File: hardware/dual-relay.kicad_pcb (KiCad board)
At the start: 2 copper layers, 45 x 45 mm, 34 parts, among them J1 AKL_5_2, J2 AKL_5_2, J3 AKL_5_2, P1 CON-SENSOR, Q1 2N7002P, Q2 2N7002P, U1 M24C64, U2 ORWH-SX, U3 ORWH-SX, U4 CM1293A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

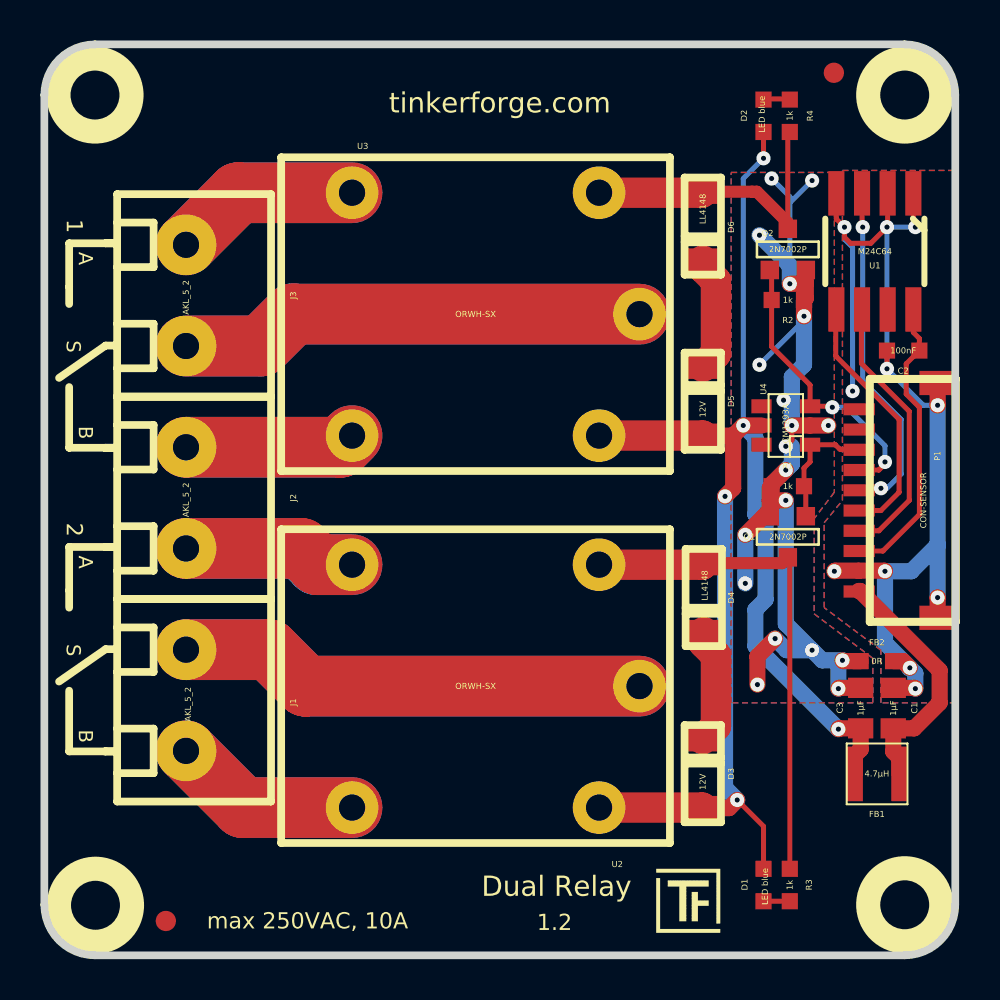
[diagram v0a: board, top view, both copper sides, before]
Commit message: change design for better production
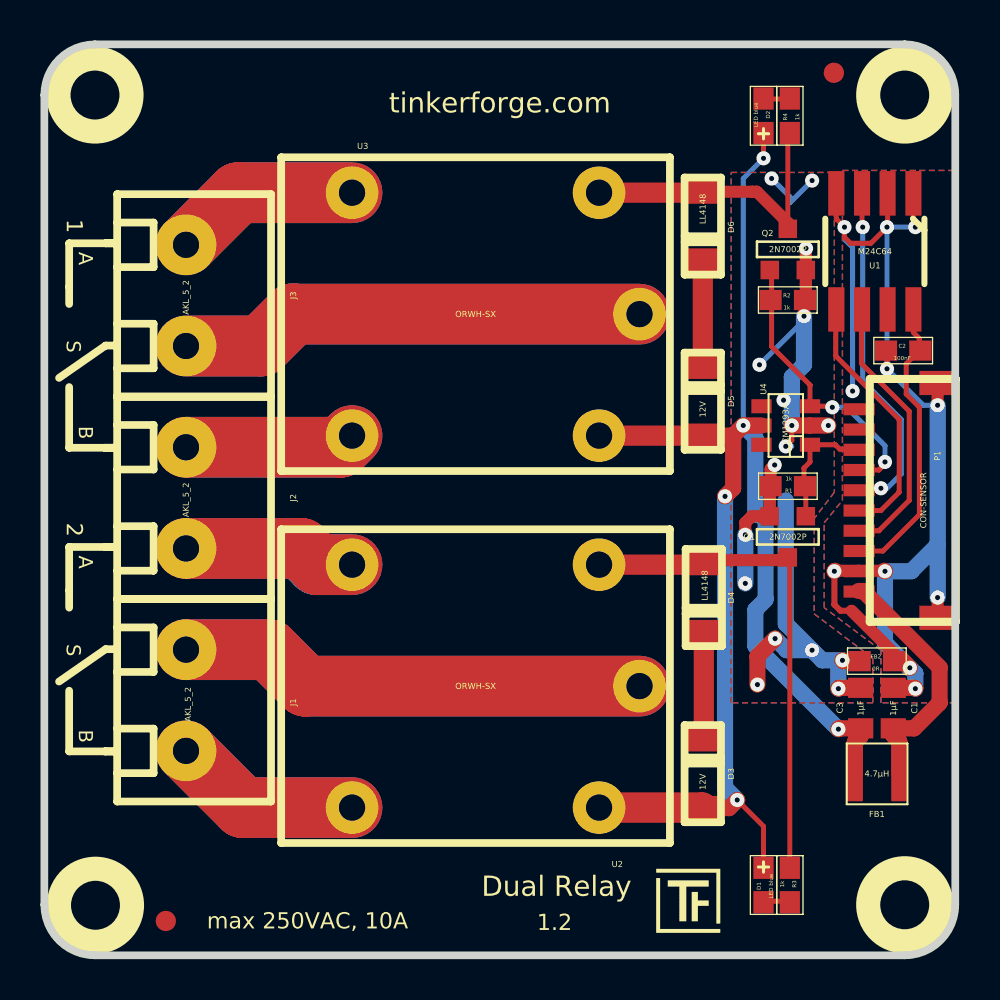
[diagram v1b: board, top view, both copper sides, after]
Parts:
- C2, FB2, R1, R2, R3, R4: footprint 0603 -> 0603E
- D1, D2: footprint D0603 -> D0603E
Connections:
- P1 pad 10: (no net) -> Net-(P1-Pad10)
- P1 pad 9: (no net) -> Net-(P1-Pad9)
- U1 pad 7: (no net) -> Net-(U1-Pad7)
- U4 pad 4: (no net) -> Net-(U4-Pad4)
- U4 pad 6: (no net) -> Net-(U4-Pad6)
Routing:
- net AGND: track 53.4 -> 42.3 mm, vias 19 -> 15
- net GND: track 54.9 -> 60.9 mm
- net (no net): track 0.00 -> 3.13 mm, vias 0 -> 2
- net Net-(D5-Pad2): track 5.79 -> 5.25 mm

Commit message: more improvements
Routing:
- net (no net): track 3.13 -> 0.00 mm, vias 2 -> 0
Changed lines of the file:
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@@
     (links 51)
     (no_connects 0)
-    (area 126.883159 81.480659 172.265341 126.862841)
+    (area 126.220699 80.820739 282.295282 165.089523)
     (thickness 1.6002)
     (drawings 43)
-    (tracks 275)
+    (tracks 270)
     (zones 0)
     (modules 34)
@@
   )
   (layers
-    (0 Vorderseite signal)
-    (31 Rückseite signal hide)
+    (0 Vorderseite signal hide)
+    (31 Rückseite signal)
     (32 B.Adhes user)
     (33 F.Adhes user)
@@
   )
   (setup
-    (last_trace_width 0.59944)
+    (last_trace_width 0.24892)
     (user_trace_width 0.29972)
     (user_trace_width 0.59944)
@@
       (excludeedgelayer true)
       (linewidth 0.150000)
-      (plotframeref true)
+      (plotframeref false)
       (viasonmask false)
       (mode 1)
@@
     (effects (font (size 1.00076 1.00076) (thickness 0.14986)))
   )
-  (segment (start 163.9 89.5) (end 165 88.4) (width 0.24892) (layer Rückseite) (net 0))
-  (via (at 165 88.4) (size 0.70104) (layers Vorderseite Rückseite) (net 0))
-  (segment (start 163.9 89.5) (end 163.9 89.2) (width 0.24892) (layer Rückseite) (net 0))
-  (via (at 163 88.3) (size 0.70104) (layers Vorderseite Rückseite) (net 0))
-  (segment (start 163.9 89.2) (end 163 88.3) (width 0.24892) (layer Rückseite) (net 0))
   (segment (start 162.7 109.1) (end 162.2 109.6) (width 0.8001) (layer Rückseite) (net 1))
   (segment (start 162.7 105.3) (end 162.7 109.1) (width 0.8001) (layer Rückseite) (net 1))
@@
   (segment (start 167.4 115.85) (end 167.4 115.46076) (width 0.8001) (layer Vorderseite) (net 1))
   (segment (start 167.11018 116.13982) (end 167.4 115.85) (width 0.8001) (layer Vorderseite) (net 1))
-  (segment (start 154.47608 119.37448) (end 159.57522 119.37448) (width 1.50114) (layer Vorderseite) (net 1))
+  (segment (start 154.47608 119.37448) (end 159.57522 119.37448) (width 1.00076) (layer Vorderseite) (net 1))
   (segment (start 154.47608 100.99948) (end 159.59978 100.99948) (width 1.00076) (layer Vorderseite) (net 1))
   (segment (start 166.3 115.5) (end 166.3 115.5) (width 0.8001) (layer Rückseite) (net 1))
@@
   (segment (start 160.7 118.4) (end 160.7 104) (width 0.8001) (layer Rückseite) (net 1))
   (segment (start 159.6 119.39926) (end 160.90074 119.39926) (width 0.8001) (layer Vorderseite) (net 1))
-  (segment (start 159.57522 119.37448) (end 159.6 119.39926) (width 1.50114) (layer Vorderseite) (net 1))
+  (segment (start 159.57522 119.37448) (end 159.6 119.39926) (width 1.00076) (layer Vorderseite) (net 1))
   (segment (start 159.6 100.99926) (end 161.10074 100.99926) (width 0.8001) (layer Vorderseite) (net 1))
   (segment (start 159.59978 100.99948) (end 159.6 100.99926) (width 1.00076) (layer Vorderseite) (net 1))

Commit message: Add 3d information (final)
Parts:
- C1, C3: footprint 0805 -> kicad-libraries:C0805
- C2, FB2: footprint 0603E -> kicad-libraries:C0603E
- D1, D2: footprint D0603E -> kicad-libraries:D0603E
- D3, D4, D5, D6: footprint MiniMelf -> kicad-libraries:MiniMelf
- FB1: footprint NRH3015 -> kicad-libraries:NRH3015
- J1, J2, J3: footprint AKL_5_2 -> kicad-libraries:AKL_5_2
- P1: footprint CON-SENSOR -> kicad-libraries:CON-SENSOR
- Q1, Q2: footprint SOT23GDS -> kicad-libraries:SOT23GDS
- R1, R2, R3, R4: footprint 0603E -> kicad-libraries:R0603E
- U1: footprint SO-8 -> kicad-libraries:SO-8
- U2, U3: footprint ORWH-SX -> kicad-libraries:ORWH-SX
- U4: footprint SC-74 -> kicad-libraries:SC-74
- U5, U6, U7, U8: footprint DRILL_NP -> kicad-libraries:DRILL_NP
